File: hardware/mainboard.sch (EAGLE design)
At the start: 64 parts, among them J1 AVR_SPI_PROG_3X2TESTPOINTS, Q1 220mA/50V/3.5Ω, Q2 220mA/50V/3.5Ω, Q3 220mA/50V/3.5Ω, U1 ATTINY861V-10MU

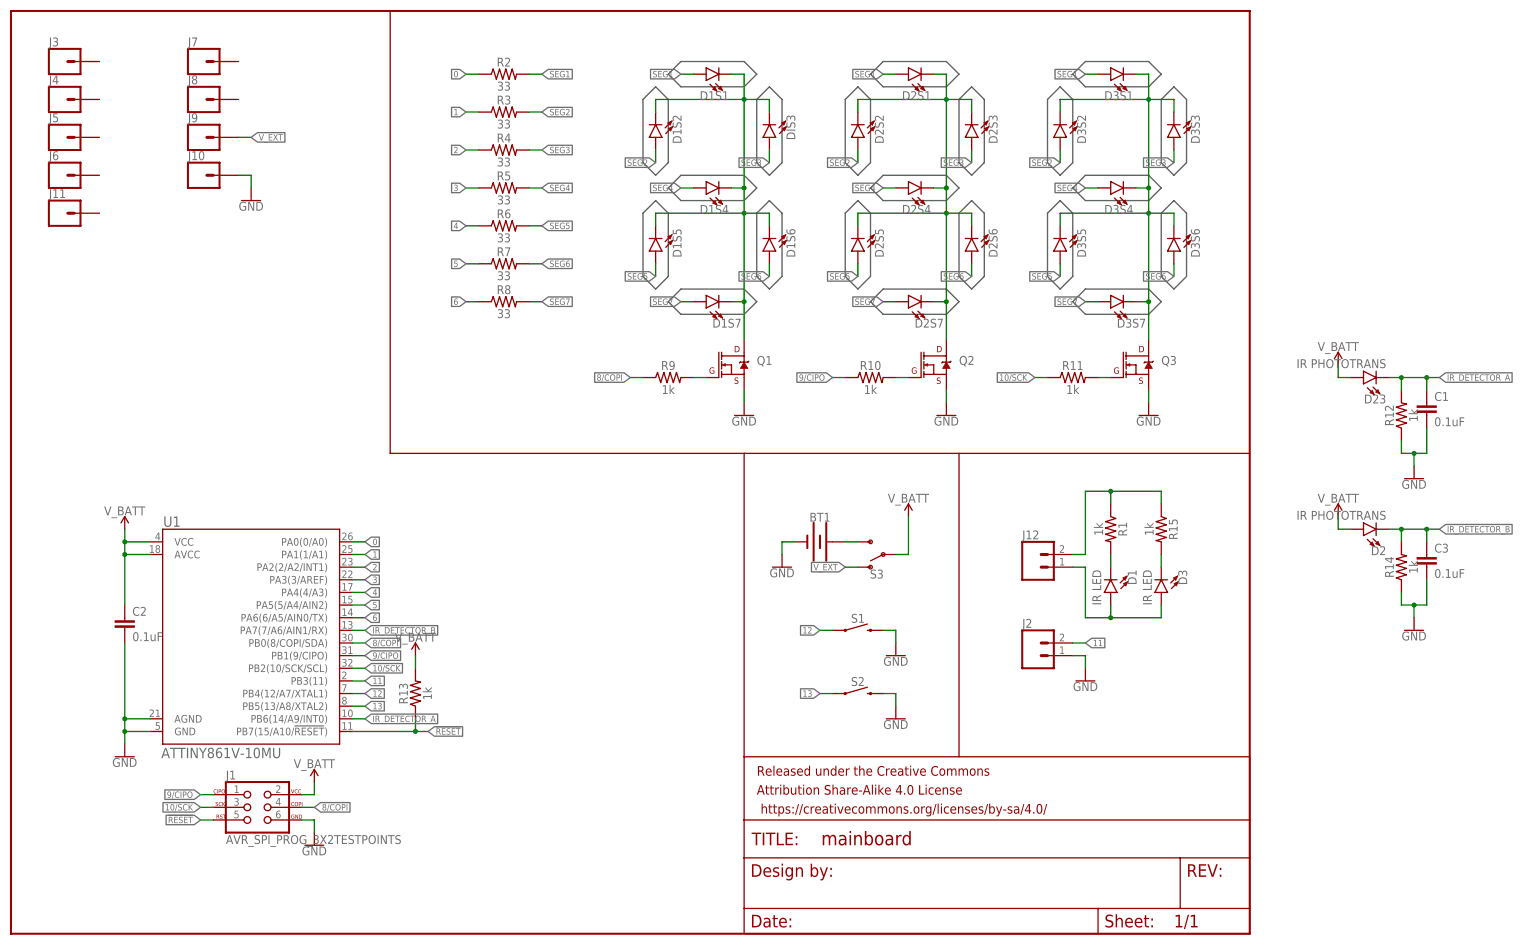
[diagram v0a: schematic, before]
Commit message: Housekeeping
- Remove prototypes
- Remove EAGLE backup files
- Archive GHPages site
- Commit 3D CAD
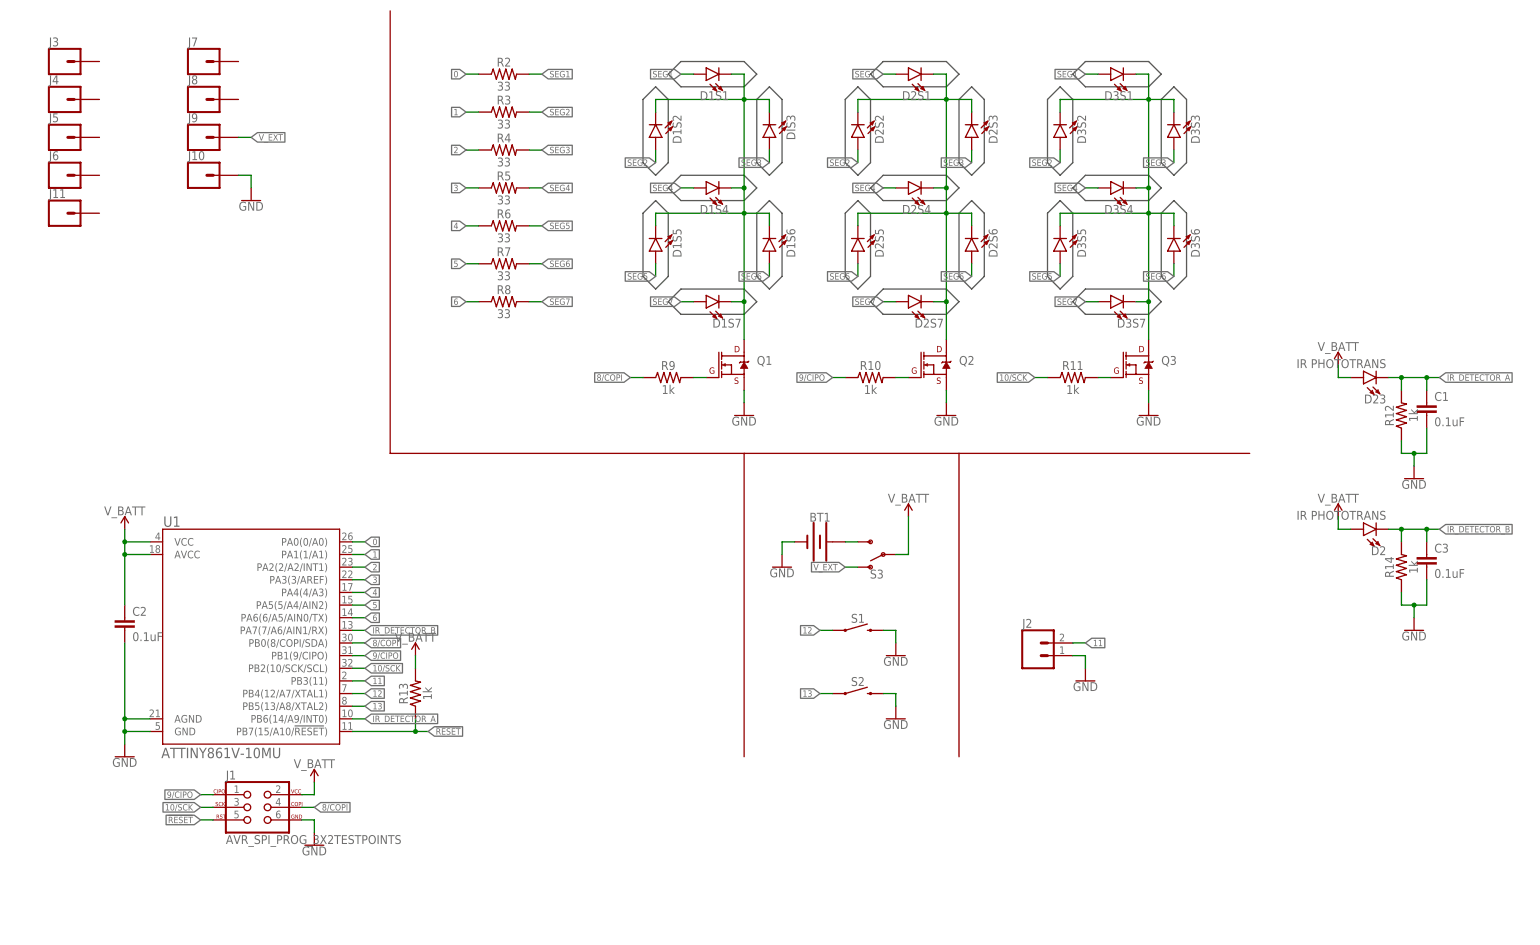
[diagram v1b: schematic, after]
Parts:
- removed D1, D3: IR LED, SparkFun-LED:LED-IR0603
- removed FRAME1: FRAME-LETTER, SparkFun-Aesthetics:FRAME-LETTER
- removed J12: (no value), SparkFun-Connectors:CONN_02
- removed R1, R15: 1k, SparkFun-Resistors:1KOHM-0603-1/10W-1%
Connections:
- removed net N$44: J12.2, R1.1, R15.1
- removed net N$45: D1.C, R1.2
- removed net N$46: D3.C, R15.2
- removed net N$51: D1.A, D3.A, J12.1
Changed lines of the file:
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@@
 <?xml version="1.0" encoding="utf-8"?>
 <!DOCTYPE eagle SYSTEM "eagle.dtd">
-<eagle version="9.5.2">
+<eagle version="9.6.2">
 <drawing>
 <settings>
@@
 </classes>
 <parts>
-<part name="FRAME1" library="SparkFun-Aesthetics" deviceset="FRAME-LETTER" device=""/>
 <part name="S1" library="SparkFun-Switches" deviceset="MOMENTARY-SWITCH-SPST" device="-SMD-5.2MM-TALL"/>
 <part name="S2" library="SparkFun-Switches" deviceset="MOMENTARY-SWITCH-SPST" device="-SMD-5.2MM-TALL"/>
@@
 <part name="J10" library="SparkFun-Connectors" deviceset="CONN_01" device=""/>
 <part name="J11" library="SparkFun-Connectors" deviceset="CONN_01" device=""/>
-<part name="J12" library="SparkFun-Connectors" deviceset="CONN_02" device=""/>
-<part name="R1" library="SparkFun-Resistors" deviceset="1KOHM" device="-0603-1/10W-1%" value="1k"/>
-<part name="D1" library="SparkFun-LED" deviceset="LED-IR" device="0603" value="IR LED"/>
 <part name="GND11" library="SparkFun-PowerSymbols" deviceset="GND" device=""/>
 <part name="D2" library="SparkFun-LED" deviceset="LED-IR" device="0603" value="IR PHOTOTRANS"/>
-<part name="D3" library="SparkFun-LED" deviceset="LED-IR" device="0603" value="IR LED"/>
 <part name="SUPPLY6" library="SparkFun-PowerSymbols" deviceset="V_BATT" device=""/>
 <part name="R14" library="SparkFun-Resistors" deviceset="1KOHM" device="-0603-1/10W-1%" value="1k"/>
 <part name="C3" library="SparkFun-Capacitors" deviceset="0.1UF" device="-0603-25V-(+80/-20%)" value="0.1uF"/>
 <part name="GND12" library="SparkFun-PowerSymbols" deviceset="GND" device=""/>
-<part name="R15" library="SparkFun-Resistors" deviceset="1KOHM" device="-0603-1/10W-1%" value="1k"/>
 </parts>
 <sheets>
@@
 </plain>
 <instances>
-<instance part="FRAME1" gate="G$1" x="0" y="0" smashed="yes"/>
-<instance part="FRAME1" gate="V" x="147.32" y="0" smashed="yes">
-<attribute name="LAST_DATE_TIME" x="160.02" y="1.27" size="2.54" layer="94" font="vector"/>
-<attribute name="SHEET" x="233.68" y="1.27" size="2.54" layer="94" font="vector"/>
-<attribute name="DRAWING_NAME" x="162.814" y="17.78" size="2.7432" layer="94" font="vector"/>
-<attribute name="DESIGNER" x="170.434" y="11.176" size="2.7432" layer="94" font="vector"/>
-<attribute name="REV" x="236.22" y="6.604" size="2.7432" layer="94" font="vector"/>
-</instance>
 <instance part="S1" gate="G$1" x="170.18" y="60.96" smashed="yes">
 <attribute name="NAME" x="170.18" y="62.484" size="1.778" layer="95" font="vector" align="bottom-center"/>
@@
 <attribute name="NAME" x="7.62" y="147.828" size="1.778" layer="95" font="vector"/>
 </instance>
-<instance part="J12" gate="G$1" x="205.74" y="73.66" smashed="yes">
-<attribute name="VALUE" x="203.2" y="68.834" size="1.778" layer="96" font="vector"/>
-<attribute name="NAME" x="203.2" y="79.248" size="1.778" layer="95" font="vector"/>
-</instance>
-<instance part="R1" gate="G$1" x="220.98" y="81.28" smashed="yes" rot="R270">
-<attribute name="NAME" x="222.504" y="81.28" size="1.778" layer="95" font="vector" rot="R270" align="bottom-center"/>
-<attribute name="VALUE" x="219.456" y="81.28" size="1.778" layer="96" font="vector" rot="R270" align="top-center"/>
-</instance>
-<instance part="D1" gate="G$1" x="220.98" y="68.58" smashed="yes" rot="R180">
-<attribute name="NAME" x="224.409" y="73.152" size="1.778" layer="95" font="vector" rot="R270"/>
-<attribute name="VALUE" x="219.075" y="73.152" size="1.778" layer="96" font="vector" rot="R270" align="top-left"/>
-</instance>
 <instance part="GND11" gate="1" x="48.26" y="147.32" smashed="yes">
 <attribute name="VALUE" x="48.26" y="147.066" size="1.778" layer="96" align="top-center"/>
@@
 <attribute name="VALUE" x="276.352" y="83.185" size="1.778" layer="96" font="vector" rot="R180" align="top-left"/>
 </instance>
-<instance part="D3" gate="G$1" x="231.14" y="68.58" smashed="yes" rot="R180">
-<attribute name="NAME" x="234.569" y="73.152" size="1.778" layer="95" font="vector" rot="R270"/>
-<attribute name="VALUE" x="229.235" y="73.152" size="1.778" layer="96" font="vector" rot="R270" align="top-left"/>
-</instance>
 <instance part="SUPPLY6" gate="G$1" x="266.7" y="83.82" smashed="yes">
 <attribute name="VALUE" x="266.7" y="86.614" size="1.778" layer="96" align="bottom-center"/>
@@
 <instance part="GND12" gate="1" x="281.94" y="60.96" smashed="yes">
 <attribute name="VALUE" x="281.94" y="60.706" size="1.778" layer="96" align="top-center"/>
-</instance>
-<instance part="R15" gate="G$1" x="231.14" y="81.28" smashed="yes" rot="R270">
-<attribute name="NAME" x="232.664" y="81.28" size="1.778" layer="95" font="vector" rot="R270" align="bottom-center"/>
-<attribute name="VALUE" x="229.616" y="81.28" size="1.778" layer="96" font="vector" rot="R270" align="top-center"/>
 </instance>
 </instances>
@@
 </segment>
 </net>
-<net name="N$44" class="0">
-<segment>
-<pinref part="R1" gate="G$1" pin="1"/>
-<wire x1="220.98" y1="86.36" x2="220.98" y2="88.9" width="0.1524" layer="91"/>
-<wire x1="220.98" y1="88.9" x2="231.14" y2="88.9" width="0.1524" layer="91"/>
-<pinref part="R15" gate="G$1" pin="1"/>
-<wire x1="231.14" y1="88.9" x2="231.14" y2="86.36" width="0.1524" layer="91"/>
-<wire x1="220.98" y1="88.9" x2="215.9" y2="88.9" width="0.1524" layer="91"/>
-<wire x1="215.9" y1="88.9" x2="215.9" y2="76.2" width="0.1524" layer="91"/>
-<junction x="220.98" y="88.9"/>
-<pinref part="J12" gate="G$1" pin="2"/>
-<wire x1="215.9" y1="76.2" x2="213.36" y2="76.2" width="0.1524" layer="91"/>
-</segment>
-</net>
-<net name="N$45" class="0">
-<segment>
-<pinref part="R1" gate="G$1" pin="2"/>
-<pinref part="D1" gate="G$1" pin="C"/>
-<wire x1="220.98" y1="76.2" x2="220.98" y2="73.66" width="0.1524" layer="91"/>
-</segment>
-</net>
-<net name="N$46" class="0">
-<segment>
-<pinref part="R15" gate="G$1" pin="2"/>
-<pinref part="D3" gate="G$1" pin="C"/>
-<wire x1="231.14" y1="76.2" x2="231.14" y2="73.66" width="0.1524" layer="91"/>
-</segment>
-</net>
-<net name="N$51" class="0">
-<segment>
-<pinref part="D1" gate="G$1" pin="A"/>
-<wire x1="220.98" y1="66.04" x2="220.98" y2="63.5" width="0.1524" layer="91"/>
-<wire x1="220.98" y1="63.5" x2="231.14" y2="63.5" width="0.1524" layer="91"/>
-<pinref part="D3" gate="G$1" pin="A"/>
-<wire x1="231.14" y1="63.5" x2="231.14" y2="66.04" width="0.1524" layer="91"/>
-<wire x1="220.98" y1="63.5" x2="215.9" y2="63.5" width="0.1524" layer="91"/>
-<wire x1="215.9" y1="63.5" x2="215.9" y2="73.66" width="0.1524" layer="91"/>
-<junction x="220.98" y="63.5"/>
-<pinref part="J12" gate="G$1" pin="1"/>
-<wire x1="215.9" y1="73.66" x2="213.36" y2="73.66" width="0.1524" layer="91"/>
-</segment>
-</net>
